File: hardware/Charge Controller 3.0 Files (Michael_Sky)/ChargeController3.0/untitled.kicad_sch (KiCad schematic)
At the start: 3 parts, among them J1 Conn_02x26_Odd_Even, J12 Conn_02x26_Odd_Even, J20 Conn_01x08_Pin

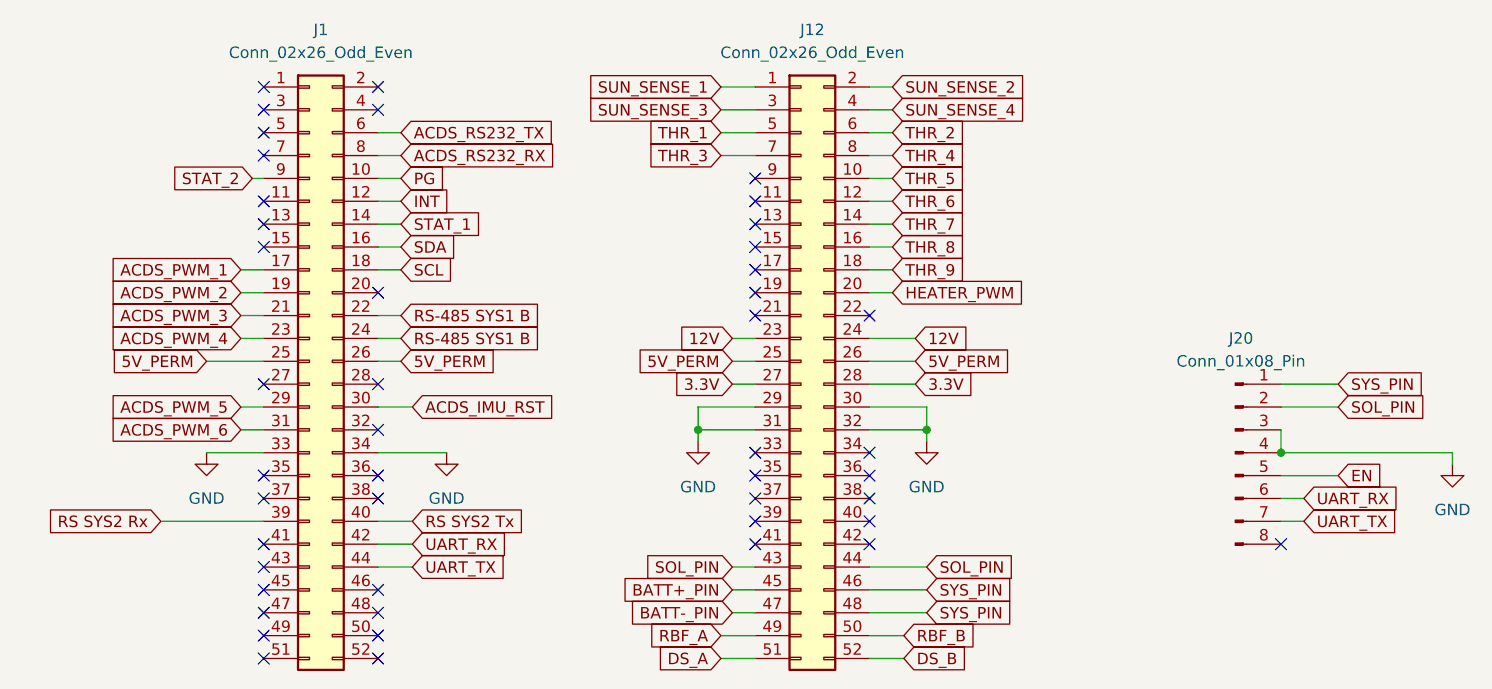
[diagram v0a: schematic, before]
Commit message: pc104 pinout fixes
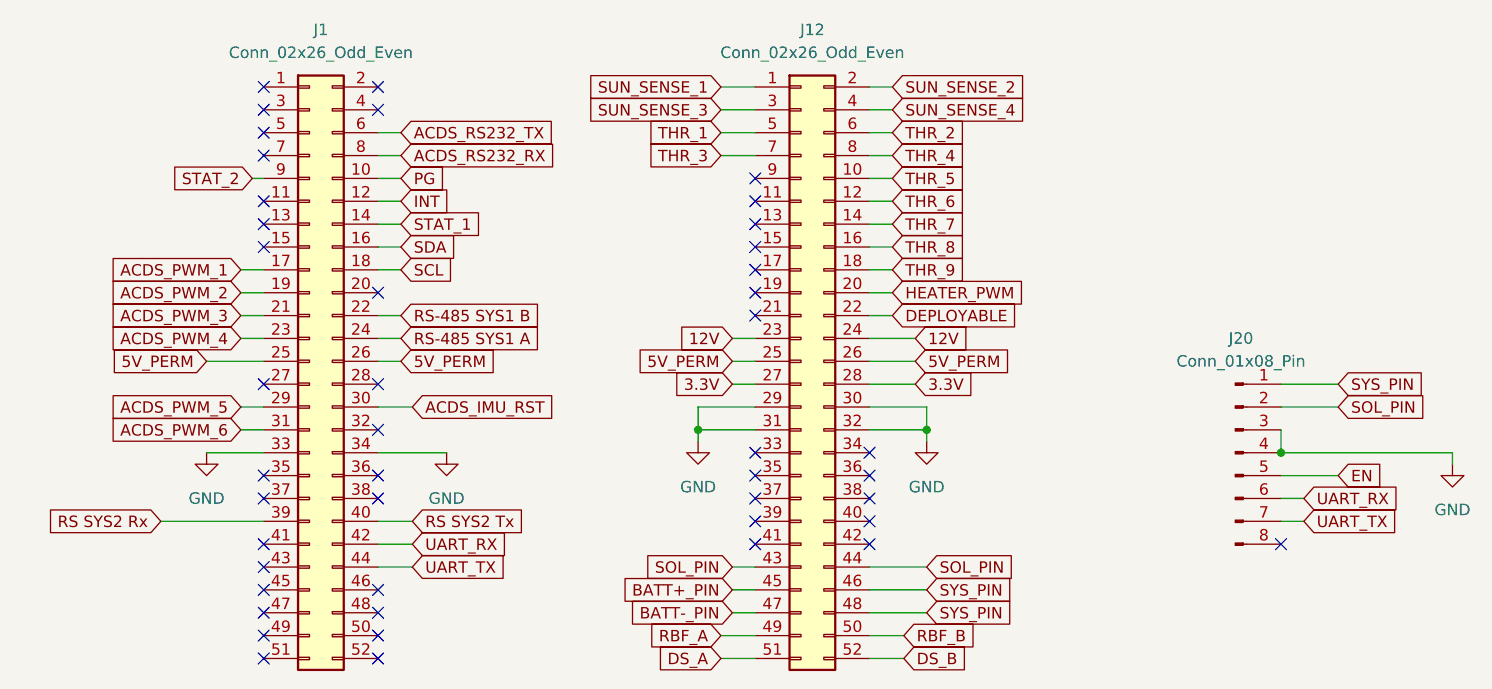
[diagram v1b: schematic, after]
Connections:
- net RS-485 SYS1 B: no longer J1.24 (Pin_24)
- net DEPLOYABLE: now reaches J12.22 (Pin_22)
- new net RS-485 SYS1 A: J1.24 (Pin_24)
- no-connect marks 46 -> 45
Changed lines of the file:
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@@
-	)
-	(no_connect
-		(at 167.64 80.01)
 	)
 	(no_connect
@@
 	(wire
 		(pts
+			(xy 167.64 80.01) (xy 170.18 80.01)
+		)
+		(stroke
+			(width 0)
+			(type default)
+		)
+	)
+	(wire
+		(pts
 			(xy 213.36 90.17) (xy 219.71 90.17)
 		)
@@
 		)
 	)
+	(global_label "DEPLOYABLE"
+		(shape input)
+		(at 170.18 80.01 0)
+		(fields_autoplaced yes)
+		(effects
+			(font
+				(size 1.27 1.27)
+			)
+			(justify left)
+		)
+		(property "Intersheetrefs" "${INTERSHEET_REFS}"
+			(at 184.8371 80.01 0)
+			(hide yes)
+			(show_name no)
+			(do_not_autoplace no)
+			(effects
+				(font
+					(size 1.27 1.27)
+				)
+				(justify left)
+			)
+		)
+	)
 	(global_label "UART_TX"
 		(shape input)
@@
 		)
 	)
-	(global_label "RS-485 SYS1 B"
+	(global_label "RS-485 SYS1 A"
 		(shape input)
 		(at 115.57 82.55 0)
@@
 		)
 		(property "Intersheetrefs" "${INTERSHEET_REFS}"
-			(at 134.1579 82.55 0)
-			(hide yes)
-			(show_name no)
+			(at 133.9765 82.55 0)
+			(hide yes)
+			(show_name no)
